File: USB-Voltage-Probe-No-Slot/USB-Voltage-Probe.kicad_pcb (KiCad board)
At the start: 2 copper layers, 30.5 x 17.8 mm, 4 parts, among them J1 USB3_A, J2 USB3_A, J3 GND, J4 VBUS

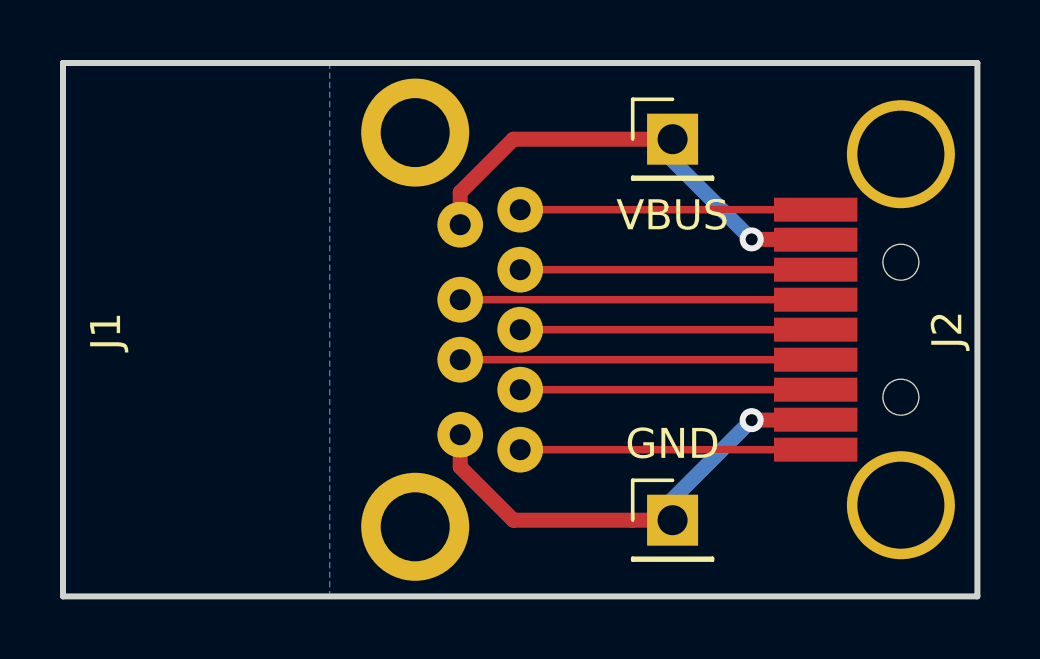
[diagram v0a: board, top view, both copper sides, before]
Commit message: Changed stuff to work better on oshpark board constraints
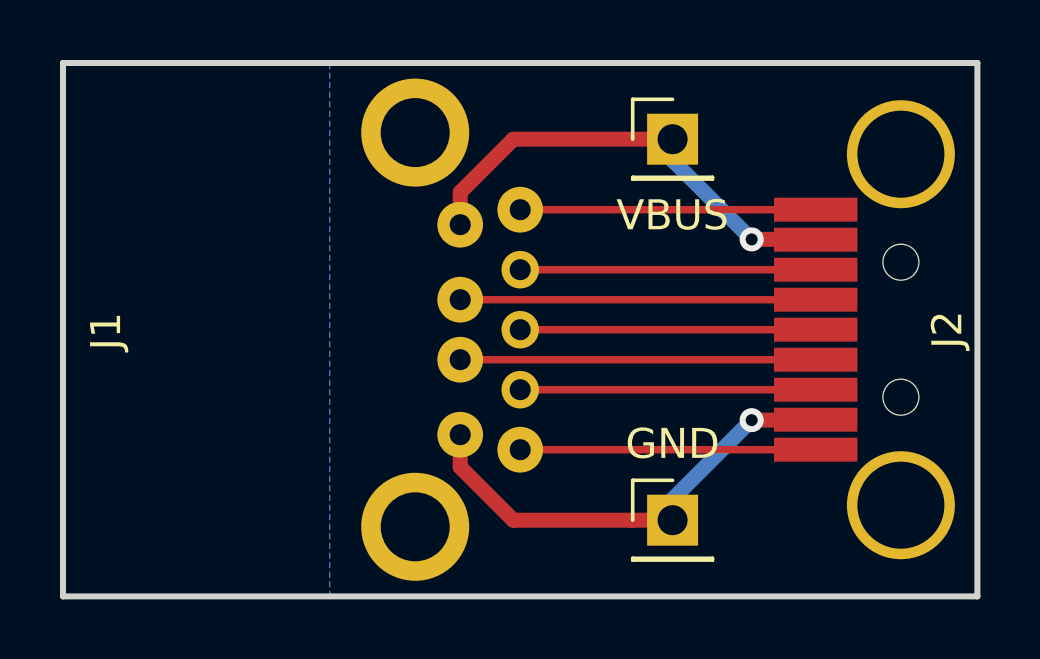
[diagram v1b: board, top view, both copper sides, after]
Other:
- net class Default: clearance 0.1 -> 0.2
- net class Power: clearance 0.1 -> 0.2
- rule trace_clearance: 0.1 -> 0.2
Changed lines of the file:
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@@
-(kicad_pcb (version 20171130) (host pcbnew "(5.0-dev-4115-gdd04bcb)")
+(kicad_pcb (version 20171130) (host pcbnew "(5.0.0-rc2-110-g9edfd25)")
   (general
     (thickness 1.6)
@@
   (setup
     (last_trace_width 0.25)
-    (trace_clearance 0.1)
+    (trace_clearance 0.2)
     (zone_clearance 0.25)
     (zone_45_only no)
@@
       (hpglpennumber 1)
       (hpglpenspeed 20)
-      (hpglpendiameter 15)
+      (hpglpendiameter 15.000000)
       (psnegative false)
       (psa4output false)
@@
   (net 10 "Net-(J1-Pad10)")
   (net_class Default "This is the default net class."
-    (clearance 0.1)
+    (clearance 0.2)
     (trace_width 0.25)
     (via_dia 0.8)
@@
   )
   (net_class Power ""
-    (clearance 0.1)
+    (clearance 0.2)
     (trace_width 0.5)
     (via_dia 0.8)
@@
     (add_net "Net-(J1-Pad1)")
     (add_net "Net-(J1-Pad4)")
+  )
+  (module USB3_A_Connector:USB_3_A_Recepticle_Amphenol_10117835-002LF_NoSlot (layer F.Cu)
+    (at 143.01 54.61 270)
+    (fp_text reference J1 (at 0.05 6.95 270) (layer F.SilkS)
+      (effects (font (size 1 1) (thickness 0.15)))
+    )
+    (fp_text value USB3_A (at 0.1 -11.4 270) (layer F.Fab)
+      (effects (font (size 1 1) (thickness 0.15)))
+    )
+    (fp_line (start -7.95 8.35) (end -7.95 -8.35) (layer F.CrtYd) (width 0.05))
+    (fp_line (start -7.95 8.35) (end 7.95 8.35) (layer F.CrtYd) (width 0.05))
+    (fp_line (start 7.95 8.35) (end 7.95 -8.35) (layer F.CrtYd) (width 0.05))
+    (fp_line (start 7.95 -8.35) (end -7.95 -8.35) (layer F.CrtYd) (width 0.05))
+    (pad 10 thru_hole circle (at -6.57 -3.35 270) (size 3.6 3.6) (drill 2.3) (layers *.Cu *.Mask)
+      (net 10 "Net-(J1-Pad10)"))
+    (pad 10 thru_hole circle (at 6.57 -3.35 270) (size 3.6 3.6) (drill 2.3) (layers *.Cu *.Mask)
+      (net 10 "Net-(J1-Pad10)"))
+    (pad 4 thru_hole circle (at 3.5 -4.85 270) (size 1.524 1.524) (drill 0.7) (layers *.Cu *.Mask)
+      (net 9 "Net-(J1-Pad4)"))
+    (pad 3 thru_hole circle (at 1 -4.85 270) (size 1.524 1.524) (drill 0.7) (layers *.Cu *.Mask)
+      (net 8 "Net-(J1-Pad3)"))
+    (pad 2 thru_hole circle (at -1 -4.85 270) (size 1.524 1.524) (drill 0.7) (layers *.Cu *.Mask)
+      (net 7 "Net-(J1-Pad2)"))
+    (pad 1 thru_hole circle (at -3.5 -4.85 270) (size 1.524 1.524) (drill 0.7) (layers *.Cu *.Mask)
+      (net 6 "Net-(J1-Pad1)"))
+    (pad 5 thru_hole circle (at 4 -6.85 270) (size 1.524 1.524) (drill 0.7) (layers *.Cu *.Mask)
+      (net 5 "Net-(J1-Pad5)"))
+    (pad 6 thru_hole circle (at 2 -6.85 270) (size 1.25 1.25) (drill 0.7) (layers *.Cu *.Mask)
+      (net 4 "Net-(J1-Pad6)"))
+    (pad 9 thru_hole circle (at -4 -6.85 270) (size 1.524 1.524) (drill 0.7) (layers *.Cu *.Mask)
+      (net 3 "Net-(J1-Pad9)"))
+    (pad 8 thru_hole circle (at -2 -6.85 270) (size 1.25 1.25) (drill 0.7) (layers *.Cu *.Mask)
+      (net 2 "Net-(J1-Pad8)"))
+    (pad 7 thru_hole circle (at 0 -6.85 270) (size 1.25 1.25) (drill 0.7) (layers *.Cu *.Mask)
+      (net 1 "Net-(J1-Pad7)"))
   )
   (module Pin_Headers:Pin_Header_Straight_1x01_Pitch2.54mm (layer F.Cu)
@@
     )
   )
-  (module USB3_A_Connector:USB_3_A_Recepticle_Amphenol_10117835-002LF_NoSlot (layer F.Cu)
-    (at 143.01 54.61 270)
-    (fp_text reference J1 (at 0.05 6.95 270) (layer F.SilkS)
-      (effects (font (size 1 1) (thickness 0.15)))
-    )
-    (fp_text value USB3_A (at 0.1 -11.4 270) (layer F.Fab)
-      (effects (font (size 1 1) (thickness 0.15)))
-    )
-    (fp_line (start 7.95 -8.35) (end -7.95 -8.35) (layer F.CrtYd) (width 0.05))
-    (fp_line (start 7.95 8.35) (end 7.95 -8.35) (layer F.CrtYd) (width 0.05))
-    (fp_line (start -7.95 8.35) (end 7.95 8.35) (layer F.CrtYd) (width 0.05))
-    (fp_line (start -7.95 8.35) (end -7.95 -8.35) (layer F.CrtYd) (width 0.05))
-    (pad 7 thru_hole circle (at 0 -6.85 270) (size 1.524 1.524) (drill 0.7) (layers *.Cu *.Mask)
-      (net 1 "Net-(J1-Pad7)"))
-    (pad 8 thru_hole circle (at -2 -6.85 270) (size 1.524 1.524) (drill 0.7) (layers *.Cu *.Mask)
-      (net 2 "Net-(J1-Pad8)"))
-    (pad 9 thru_hole circle (at -4 -6.85 270) (size 1.524 1.524) (drill 0.7) (layers *.Cu *.Mask)
-      (net 3 "Net-(J1-Pad9)"))
-    (pad 6 thru_hole circle (at 2 -6.85 270) (size 1.524 1.524) (drill 0.7) (layers *.Cu *.Mask)
-      (net 4 "Net-(J1-Pad6)"))
-    (pad 5 thru_hole circle (at 4 -6.85 270) (size 1.524 1.524) (drill 0.7) (layers *.Cu *.Mask)
-      (net 5 "Net-(J1-Pad5)"))
-    (pad 1 thru_hole circle (at -3.5 -4.85 270) (size 1.524 1.524) (drill 0.7) (layers *.Cu *.Mask)
-      (net 6 "Net-(J1-Pad1)"))
-    (pad 2 thru_hole circle (at -1 -4.85 270) (size 1.524 1.524) (drill 0.7) (layers *.Cu *.Mask)
-      (net 7 "Net-(J1-Pad2)"))
-    (pad 3 thru_hole circle (at 1 -4.85 270) (size 1.524 1.524) (drill 0.7) (layers *.Cu *.Mask)
-      (net 8 "Net-(J1-Pad3)"))
-    (pad 4 thru_hole circle (at 3.5 -4.85 270) (size 1.524 1.524) (drill 0.7) (layers *.Cu *.Mask)
-      (net 9 "Net-(J1-Pad4)"))
-    (pad 10 thru_hole circle (at 6.57 -3.35 270) (size 3.6 3.6) (drill 2.3) (layers *.Cu *.Mask)
-      (net 10 "Net-(J1-Pad10)"))
-    (pad 10 thru_hole circle (at -6.57 -3.35 270) (size 3.6 3.6) (drill 2.3) (layers *.Cu *.Mask)
-      (net 10 "Net-(J1-Pad10)"))
-  )
   (module USB3_A_Connector:USB_3_A_Plug_Amphenol_GSB316441CEU_NoSlot (layer F.Cu)
